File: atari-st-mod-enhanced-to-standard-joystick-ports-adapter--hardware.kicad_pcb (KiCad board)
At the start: 4 copper layers, 48 parts, among them J1 Joy0/Mouse, J2 Joy1, J3 OLED 128×64, J4 Enhanced Joystick Port, J5 Joy0/Mouse, J6 Joy1, Q1 1<Vgsth<2, Low Rdson, Vds >10, Q10 1<Vgsth<2, Low Rdson, Vds >10, Q2 1<Vgsth<2, Low Rdson, Vds >10, Q3 1<Vgsth<2, Low Rdson, Vds >10, Q4 1<Vgsth<2, Low Rdson, Vds >10, Q5 1<Vgsth<2, Low Rdson, Vds >10, Q6 1<Vgsth<2, Low Rdson, Vds >10, Q7 1<Vgsth<2, Low Rdson, Vds >10, Q8 1<Vgsth<2, Low Rdson, Vds >10, Q9 1<Vgsth<2, Low Rdson, Vds >10, SW1 Reset, SW2 Selector, SW3 Activate/Change, SW4 Cancel, U1 LM4040DBZ-3

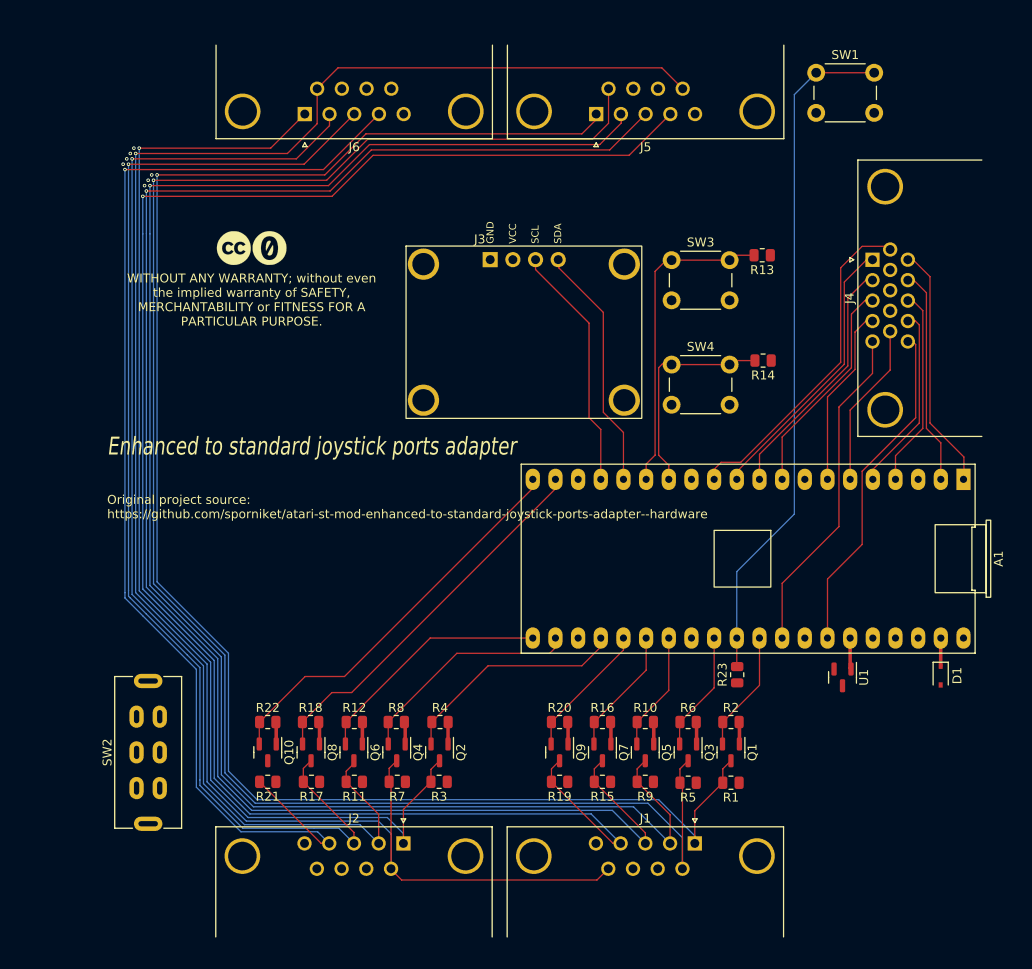
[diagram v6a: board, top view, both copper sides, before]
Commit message: PCB session 2023-02-09T07:02:41+01:00 : mounting holes, pcb shape, 3v3 copper pour
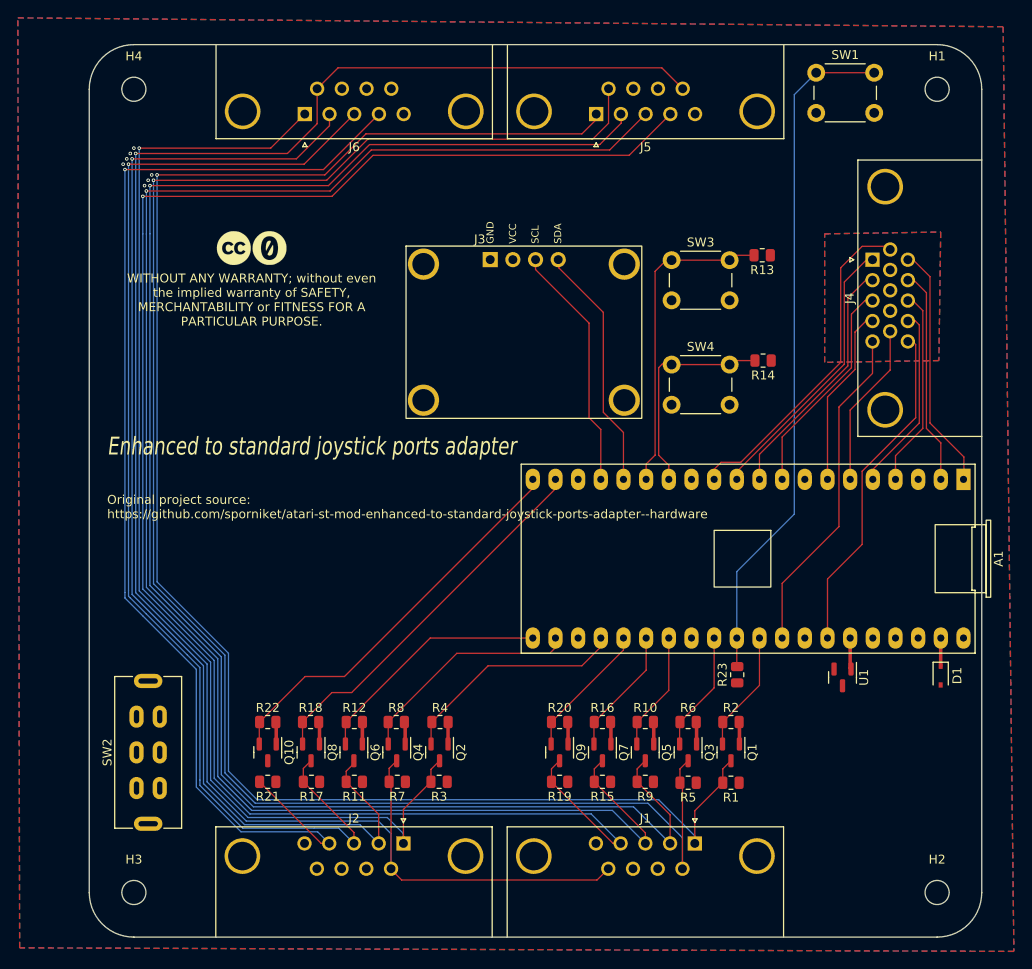
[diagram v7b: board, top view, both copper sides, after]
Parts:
- added H1: M2.5, MountingHole:MountingHole_2.7mm_M2.5, F.Cu at (145.0, 55.0)
- added H2: M2.5, MountingHole:MountingHole_2.7mm_M2.5, F.Cu at (145.0, 145.0)
- added H3: M2.5, MountingHole:MountingHole_2.7mm_M2.5, F.Cu at (55.0, 145.0)
- added H4: M2.5, MountingHole:MountingHole_2.7mm_M2.5, F.Cu at (55.0, 55.0)
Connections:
- J1 pad 0: (no net) -> GND
- J2 pad 0: (no net) -> GND
- J4 pad 0: (no net) -> GND1
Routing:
- added copper zone on B.Cu, net +3V3
- added copper zone on F.Cu, net +3V3
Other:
- board outline added: 100 x 100 mm
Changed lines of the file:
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@@
     (fp_arc (start -19.64 1.42) (mid -18.04 -0.18) (end -16.44 1.42) (layer "F.Fab") (width 0.1))
     (fp_arc (start 5.36 1.42) (mid 6.96 -0.18) (end 8.56 1.42) (layer "F.Fab") (width 0.1))
-    (pad "0" thru_hole circle (at 6.96 1.42) (size 4 4) (drill 3.2) (layers *.Cu *.Mask))
-    (pad "0" thru_hole circle (at -18.04 1.42) (size 4 4) (drill 3.2) (layers *.Cu *.Mask))
+    (pad "0" thru_hole circle (at 6.96 1.42) (size 4 4) (drill 3.2) (layers *.Cu *.Mask)
+      (net 42 "GND") (pinfunction "Shield") (pintype "passive"))
+    (pad "0" thru_hole circle (at -18.04 1.42) (size 4 4) (drill 3.2) (layers *.Cu *.Mask)
+      (net 42 "GND") (pinfunction "Shield") (pintype "passive"))
     (pad "1" thru_hole rect (at 0 0) (size 1.6 1.6) (drill 1) (layers *.Cu *.Mask)
       (net 35 "/j0_up") (pinfunction "Pin_1") (pintype "passive"))
@@
       (rotate (xyz 0 0 0))
     )
+  )
+  (footprint "MountingHole:MountingHole_2.7mm_M2.5" (layer "F.Cu")
+    (at 145 55)
+    (descr "Mounting Hole 2.7mm, no annular, M2.5")
+    (tags "mounting hole 2.7mm no annular m2.5")
+    (property "Sheetfile" "atari-st-mod-enhanced-to-standard-joystick-ports-adapter--hardware.kicad_sch")
+    (property "Sheetname" "")
+    (attr exclude_from_pos_files)
+    (fp_text reference "H1" (at 0 -3.7) (layer "F.SilkS")
+      (effects (font (size 1 1) (thickness 0.15)))
+    )
+    (fp_text value "M2.5" (at 0 3.7) (layer "F.Fab")
+      (effects (font (size 1 1) (thickness 0.15)))
+    )
+    (fp_text user "${REFERENCE}" (at 0 0) (layer "F.Fab")
+      (effects (font (size 1 1) (thickness 0.15)))
+    )
+    (fp_circle (center 0 0) (end 2.7 0) (layer "Cmts.User") (width 0.15) (fill none))
+    (fp_circle (center 0 0) (end 2.95 0) (layer "F.CrtYd") (width 0.05) (fill none))
+    (pad "" np_thru_hole circle (at 0 0) (size 2.7 2.7) (drill 2.7) (layers *.Cu *.Mask))
   )
   (footprint "Resistor_SMD:R_0805_2012Metric" (layer "F.Cu")
@@
     (fp_arc (start -18.415 1.42) (mid -16.815 -0.18) (end -15.215 1.42) (layer "F.Fab") (width 0.1))
     (fp_arc (start 6.585 1.42) (mid 8.185 -0.18) (end 9.785 1.42) (layer "F.Fab") (width 0.1))
-    (pad "0" thru_hole circle (at 8.185 1.42 90) (size 4 4) (drill 3.2) (layers *.Cu *.Mask))
-    (pad "0" thru_hole circle (at -16.815 1.42 90) (size 4 4) (drill 3.2) (layers *.Cu *.Mask))
+    (pad "0" thru_hole circle (at 8.185 1.42 90) (size 4 4) (drill 3.2) (layers *.Cu *.Mask)
+      (net 3 "GND1") (pinfunction "Shield") (pintype "passive"))
+    (pad "0" thru_hole circle (at -16.815 1.42 90) (size 4 4) (drill 3.2) (layers *.Cu *.Mask)
+      (net 3 "GND1") (pinfunction "Shield") (pintype "passive"))
     (pad "1" thru_hole rect (at 0 0 90) (size 1.6 1.6) (drill 1) (layers *.Cu *.Mask)
       (net 16 "/jag_col1") (pinfunction "Pin_1") (pintype "passive"))
@@
     (fp_arc (start 5.36 1.42) (mid 6.96 -0.18) (end 8.56 1.42) (layer "F.Fab") (width 0.1))
     (fp_arc (start -19.64 1.42) (mid -18.04 -0.18) (end -16.44 1.42) (layer "F.Fab") (width 0.1))
-    (pad "0" thru_hole circle (at -18.04 1.42) (size 4 4) (drill 3.2) (layers *.Cu *.Mask))
-    (pad "0" thru_hole circle (at 6.96 1.42) (size 4 4) (drill 3.2) (layers *.Cu *.Mask))
+    (pad "0" thru_hole circle (at -18.04 1.42) (size 4 4) (drill 3.2) (layers *.Cu *.Mask)
+      (net 42 "GND") (pinfunction "Shield") (pintype "passive"))
+    (pad "0" thru_hole circle (at 6.96 1.42) (size 4 4) (drill 3.2) (layers *.Cu *.Mask)
+      (net 42 "GND") (pinfunction "Shield") (pintype "passive"))
     (pad "1" thru_hole rect (at 0 0) (size 1.6 1.6) (drill 1) (layers *.Cu *.Mask)
       (net 44 "/j1_up") (pinfunction "Pin_1") (pintype "passive"))
@@
       (net 33 "unconnected-(A1-Pad40)") (pinfunction "VBUS") (pintype "power_in+no_connect"))
   )
+  (footprint "MountingHole:MountingHole_2.7mm_M2.5" (layer "F.Cu")
+    (at 55 55)
+    (descr "Mounting Hole 2.7mm, no annular, M2.5")
+    (tags "mounting hole 2.7mm no annular m2.5")
+    (property "Sheetfile" "atari-st-mod-enhanced-to-standard-joystick-ports-adapter--hardware.kicad_sch")
+    (property "Sheetname" "")
+    (attr exclude_from_pos_files)
+    (fp_text reference "H4" (at 0 -3.7) (layer "F.SilkS")
+      (effects (font (size 1 1) (thickness 0.15)))
+    )
+    (fp_text value "M2.5" (at 0 3.7) (layer "F.Fab")
+      (effects (font (size 1 1) (thickness 0.15)))
+    )
+    (fp_text user "${REFERENCE}" (at 0 0) (layer "F.Fab")
+      (effects (font (size 1 1) (thickness 0.15)))
+    )
+    (fp_circle (center 0 0) (end 2.7 0) (layer "Cmts.User") (width 0.15) (fill none))
+    (fp_circle (center 0 0) (end 2.95 0) (layer "F.CrtYd") (width 0.05) (fill none))
+    (pad "" np_thru_hole circle (at 0 0) (size 2.7 2.7) (drill 2.7) (layers *.Cu *.Mask))
+  )
   (footprint "Package_TO_SOT_SMD:SOT-23" (layer "F.Cu")
     (at 121.9 129.3 -90)
@@
       (rotate (xyz 0 0 0))
     )
+  )
+  (footprint "MountingHole:MountingHole_2.7mm_M2.5" (layer "F.Cu")
+    (at 55 145)
+    (descr "Mounting Hole 2.7mm, no annular, M2.5")
+    (tags "mounting hole 2.7mm no annular m2.5")
+    (property "Sheetfile" "atari-st-mod-enhanced-to-standard-joystick-ports-adapter--hardware.kicad_sch")
+    (property "Sheetname" "")
+    (attr exclude_from_pos_files)
+    (fp_text reference "H3" (at 0 -3.7) (layer "F.SilkS")
+      (effects (font (size 1 1) (thickness 0.15)))
+    )
+    (fp_text value "M2.5" (at 0 3.7) (layer "F.Fab")
+      (effects (font (size 1 1) (thickness 0.15)))
+    )
+    (fp_text user "${REFERENCE}" (at 0 0) (layer "F.Fab")
+      (effects (font (size 1 1) (thickness 0.15)))
+    )
+    (fp_circle (center 0 0) (end 2.7 0) (layer "Cmts.User") (width 0.15) (fill none))
+    (fp_circle (center 0 0) (end 2.95 0) (layer "F.CrtYd") (width 0.05) (fill none))
+    (pad "" np_thru_hole circle (at 0 0) (size 2.7 2.7) (drill 2.7) (layers *.Cu *.Mask))
   )
   (footprint "Resistor_SMD:R_0805_2012Metric" (layer "F.Cu")
@@
     )
   )
+  (footprint "MountingHole:MountingHole_2.7mm_M2.5" (layer "F.Cu")
+    (at 145 145)
+    (descr "Mounting Hole 2.7mm, no annular, M2.5")
+    (tags "mounting hole 2.7mm no annular m2.5")
+    (property "Sheetfile" "atari-st-mod-enhanced-to-standard-joystick-ports-adapter--hardware.kicad_sch")
+    (property "Sheetname" "")
+    (attr exclude_from_pos_files)
+    (fp_text reference "H2" (at 0 -3.7) (layer "F.SilkS")
+      (effects (font (size 1 1) (thickness 0.15)))
+    )
+    (fp_text value "M2.5" (at 0 3.7) (layer "F.Fab")
+      (effects (font (size 1 1) (thickness 0.15)))
+    )
+    (fp_text user "${REFERENCE}" (at 0 0) (layer "F.Fab")
+      (effects (font (size 1 1) (thickness 0.15)))
+    )
+    (fp_circle (center 0 0) (end 2.7 0) (layer "Cmts.User") (width 0.15) (fill none))
+    (fp_circle (center 0 0) (end 2.95 0) (layer "F.CrtYd") (width 0.05) (fill none))
+    (pad "" np_thru_hole circle (at 0 0) (size 2.7 2.7) (drill 2.7) (layers *.Cu *.Mask))
+  )
   (footprint "Resistor_SMD:R_0805_2012Metric" (layer "F.Cu")
     (at 107.5 125.9 180)
@@
   (gr_rect (start 50 50) (end 150 150) (layer "Dwgs.User") (width 0.15) (fill none))
   (gr_rect (start 141 141) (end 150 150) (layer "Dwgs.User") (width 0.15) (fill none))
+  (gr_arc (start 55 150) (mid 51.464466 148.535534) (end 50 145) (layer "Edge.Cuts") (width 0.1))
+  (gr_line (start 55 50) (end 145 50) (layer "Edge.Cuts") (width 0.1))
+  (gr_arc (start 50 55) (mid 51.464466 51.464466) (end 55 50) (layer "Edge.Cuts") (width 0.1))
+  (gr_line (start 50 145) (end 50 55) (layer "Edge.Cuts") (width 0.1))
+  (gr_arc (start 150 145) (mid 148.535534 148.535534) (end 145 150) (layer "Edge.Cuts") (width 0.1))
+  (gr_line (start 150 55) (end 150 145) (layer "Edge.Cuts") (width 0.1))
+  (gr_line (start 145 150) (end 55 150) (layer "Edge.Cuts") (width 0.1))
+  (gr_arc (start 145 50) (mid 148.535534 51.464466) (end 150 55) (layer "Edge.Cuts") (width 0.1))
   (gr_text "Original project source: \nhttps://github.com/sporniket/atari-st-mod-enhanced-to-standard-joystick-ports-adapter--hardware" (at 52 101.8) (layer "F.SilkS")
     (effects (font (size 1 1) (thickness 0.15)) (justify left))
@@
   (via (at 54.2 62.8) (size 0.4) (drill 0.2) (layers "F.Cu" "B.Cu") (free) (net 53))
   (via (at 53.8 63.4) (size 0.4) (drill 0.2) (layers "F.Cu" "B.Cu") (free) (net 53))
+  (zone (net 30) (net_name "+3V3") (layers F&B.Cu) (hatch edge 0.508)
+    (connect_pads (clearance 0.2))
+    (min_thickness 0.2) (filled_areas_thickness no)
+    (fill yes (thermal_gap 0.508) (thermal_bridge_width 0.508))
+    (polygon
+      (pts
+        (xy 152.4 48)
+        (xy 153.6 151.6)
+        (xy 42.2 151.2)
+        (xy 42 47)
+      )
+    )
+  )
+  (zone (net 30) (net_name "+3V3") (layers F&B.Cu) (hatch edge 0.508)
+    (connect_pads (clearance 0.2))
+    (min_thickness 0.1) (filled_areas_thickness no)
+    (fill yes (thermal_gap 0.38) (thermal_bridge_width 0.508))
+    (polygon
+      (pts
+        (xy 145.2 85.4)
+        (xy 132.4 85.6)
+        (xy 132.4 71.2)
+        (xy 145.4 71)
+      )
+    )
+  )
   (zone (net 42) (net_name "GND") (layer "In1.Cu") (hatch edge 0.508)
     (priority 1)

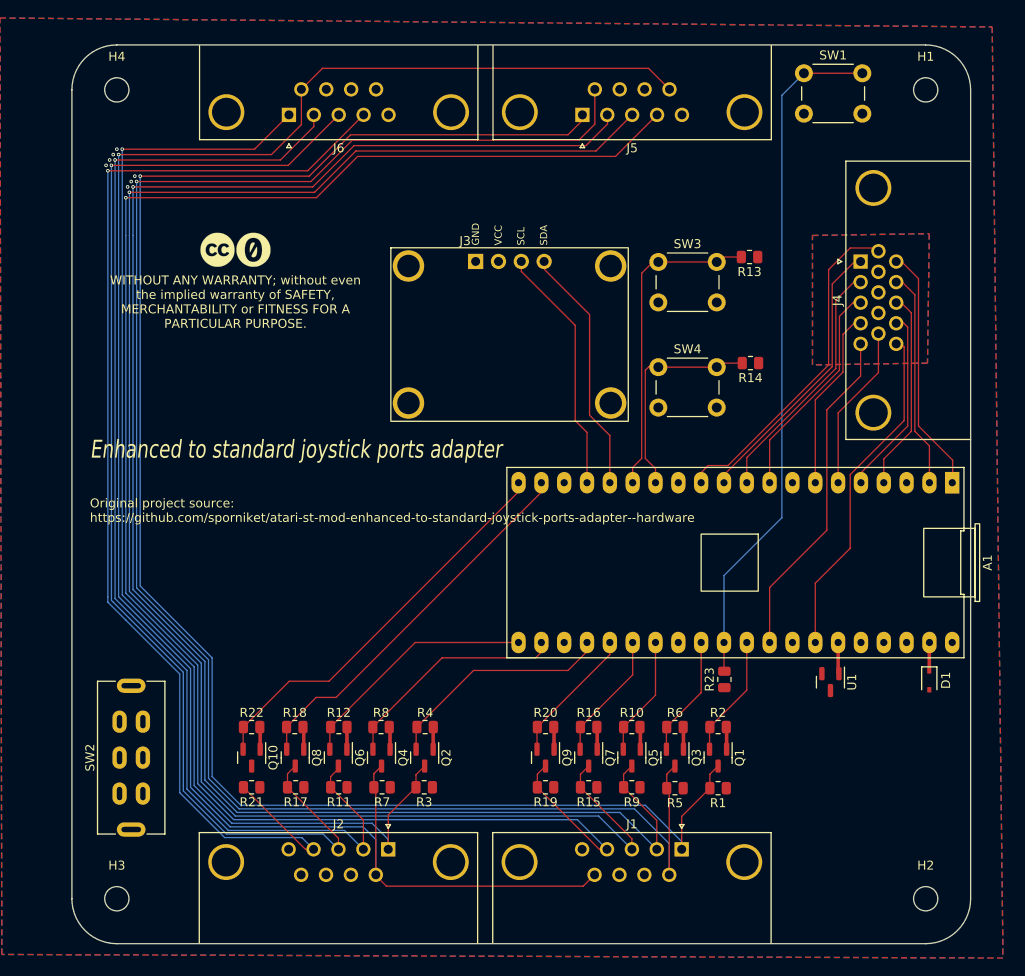
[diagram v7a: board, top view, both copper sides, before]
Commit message: PCB session 2023-02-09T09:04:18+01:00 : copper pour work
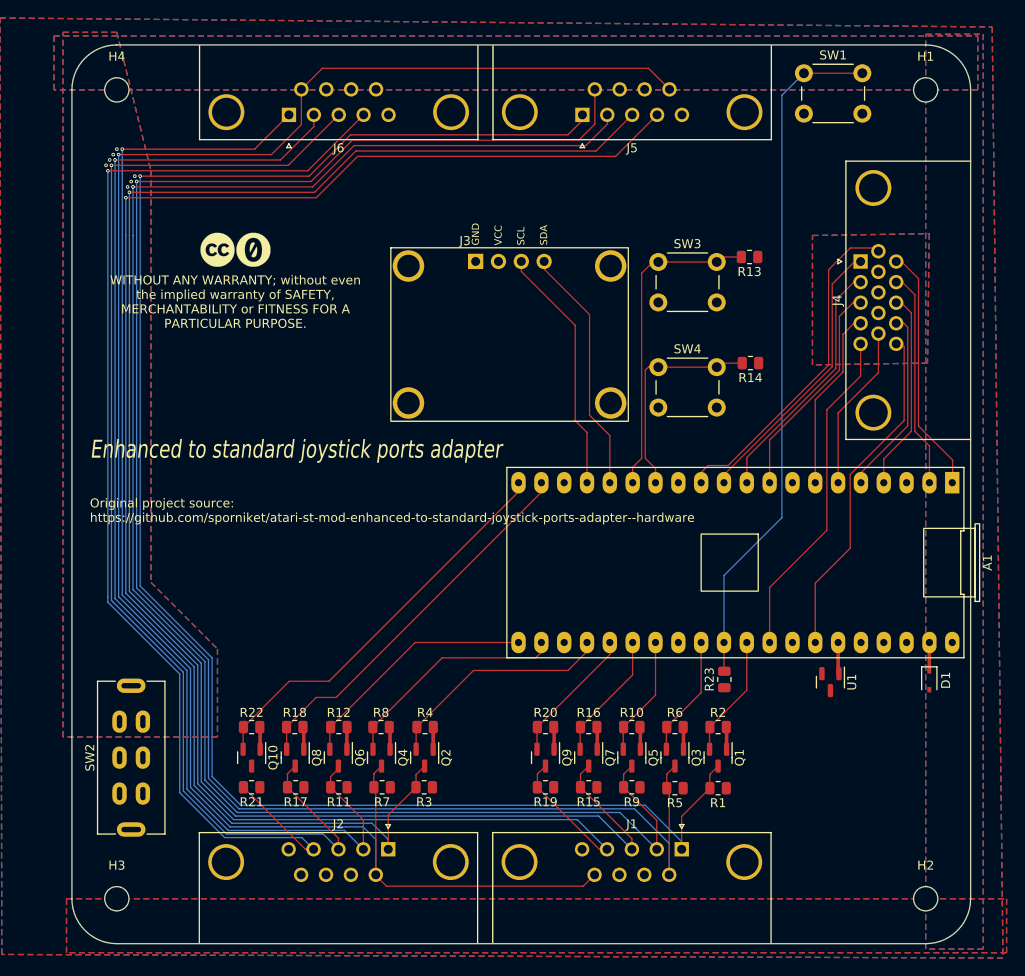
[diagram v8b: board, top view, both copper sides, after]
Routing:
- added copper zone on B.Cu, net GND1
- added copper zone on F.Cu, net GND1
- added copper zone on B.Cu, net GND2
- added copper zone on F.Cu, net GND2
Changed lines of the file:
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@@
   (via (at 54.2 62.8) (size 0.4) (drill 0.2) (layers "F.Cu" "B.Cu") (free) (net 53))
   (via (at 53.8 63.4) (size 0.4) (drill 0.2) (layers "F.Cu" "B.Cu") (free) (net 53))
+  (zone (net 3) (net_name "GND1") (layers F&B.Cu) (hatch edge 0.508)
+    (priority 1)
+    (connect_pads (clearance 0.2))
+    (min_thickness 0.2) (filled_areas_thickness no)
+    (fill yes (thermal_gap 0.508) (thermal_bridge_width 0.508))
+    (polygon
+      (pts
+        (xy 151.4 150.6)
+        (xy 145 150.6)
+        (xy 145 48.8)
+        (xy 151.4 48.8)
+      )
+    )
+  )
+  (zone (net 53) (net_name "GND2") (layers F&B.Cu) (hatch edge 0.508)
+    (priority 3)
+    (connect_pads (clearance 0.2))
+    (min_thickness 0.2) (filled_areas_thickness no)
+    (fill yes (thermal_gap 0.508) (thermal_bridge_width 0.508))
+    (polygon
+      (pts
+        (xy 58.8 64)
+        (xy 58.8 109.8)
+        (xy 66.2 117.2)
+        (xy 66.2 127)
+        (xy 49 127)
+        (xy 49 48.6)
+        (xy 55 48.6)
+      )
+    )
+  )
   (zone (net 30) (net_name "+3V3") (layers F&B.Cu) (hatch edge 0.508)
     (connect_pads (clearance 0.2))
@@
         (xy 42.2 151.2)
         (xy 42 47)
+      )
+    )
+  )
+  (zone (net 3) (net_name "GND1") (layers F&B.Cu) (hatch edge 0.508)
+    (priority 1)
+    (connect_pads (clearance 0.2))
+    (min_thickness 0.2) (filled_areas_thickness no)
+    (fill yes (thermal_gap 0.508) (thermal_bridge_width 0.508))
+    (polygon
+      (pts
+        (xy 150.8 55)
+        (xy 48 55)
+        (xy 48 49)
+        (xy 150.8 49)
       )
     )
@@
       )
     )
+  )
+  (zone (net 3) (net_name "GND1") (layers F&B.Cu) (hatch edge 0.508)
+    (priority 1)
+    (connect_pads (clearance 0.2))
+    (min_thickness 0.2) (filled_areas_thickness no)
+    (fill yes (thermal_gap 0.508) (thermal_bridge_width 0.508))
+    (polygon
+      (pts
+        (xy 154 151)
+        (xy 49.4 151)
+        (xy 49.4 145)
+        (xy 154 145)
+      )
+    )
